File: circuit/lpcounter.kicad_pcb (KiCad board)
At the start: 2 copper layers, 52.1 x 45.7 mm, 19 parts, among them IC1 ATTINY85V-P, M1 SYN115, P1 CONN_01X08, P2 CONN_02X01

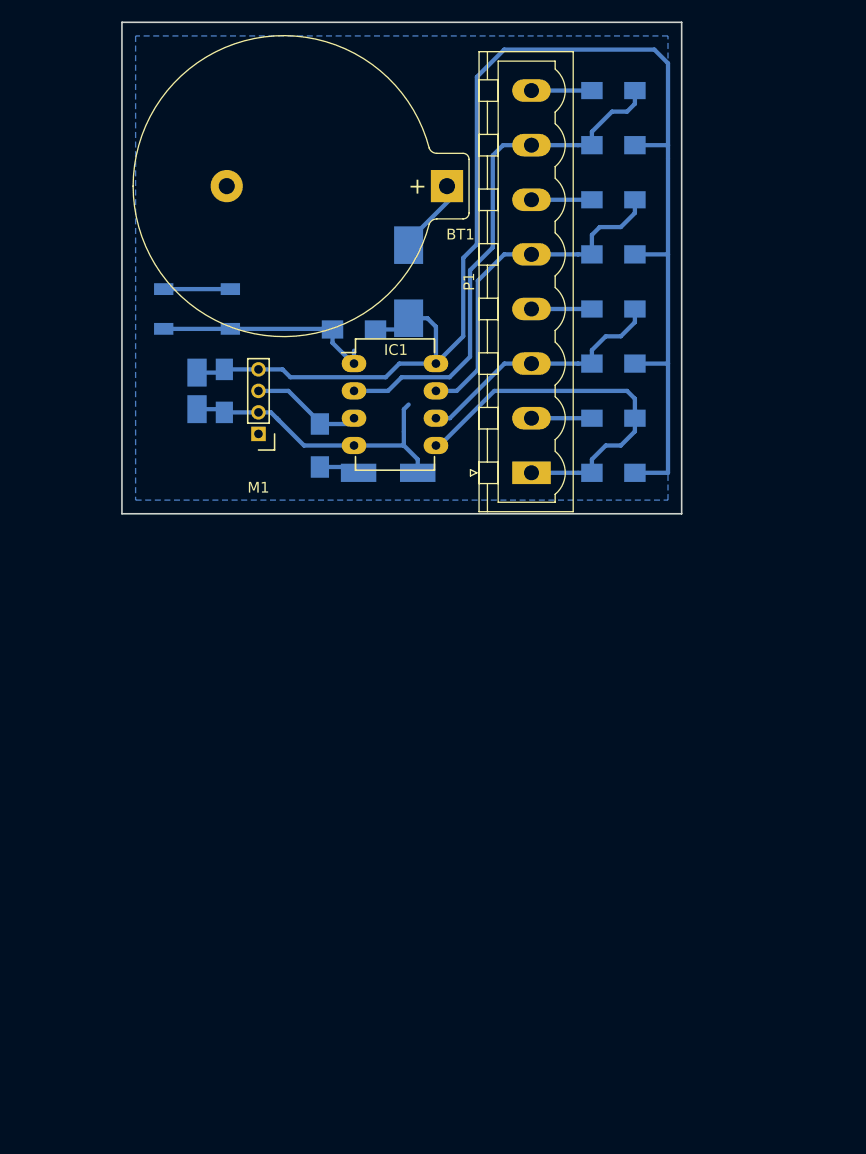
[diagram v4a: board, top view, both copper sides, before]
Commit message: correct footprint for SYN115, 4 screw holes, optimizing PCB drawing 18650 battery outiline
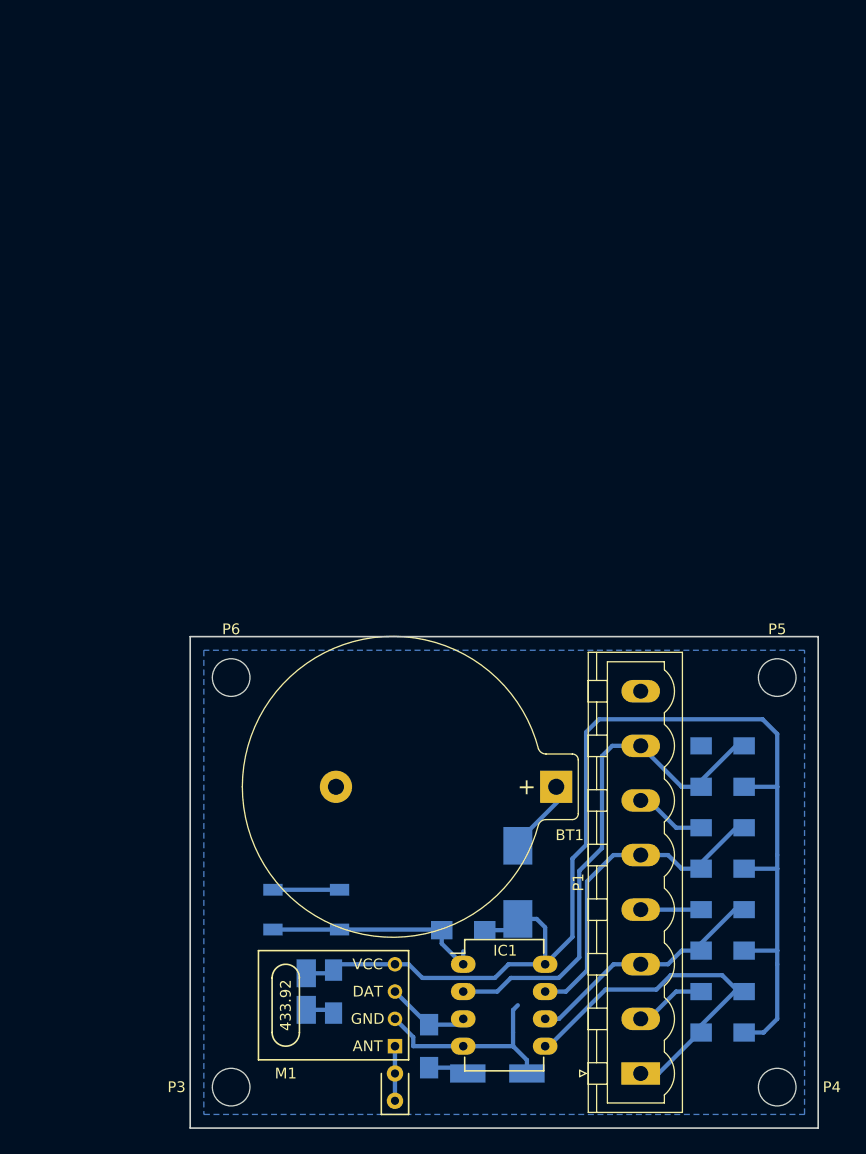
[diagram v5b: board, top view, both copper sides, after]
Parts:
- added P3: Hole_3.5mm, Mounting_Holes:MountingHole_3.5mm, F.Cu at (152.4, 119.4)
- added P4: Hole_3.5mm, Mounting_Holes:MountingHole_3.5mm, F.Cu at (203.2, 119.4)
- added P5: Hole_3.5mm, Mounting_Holes:MountingHole_3.5mm, F.Cu at (203.2, 81.3)
- added P6: Hole_3.5mm, Mounting_Holes:MountingHole_3.5mm, F.Cu at (152.4, 81.3)
- M1: footprint Pin_Headers:Pin_Header_Straight_1x04_Pitch2.00mm -> syn115:SYN115
- moved C4 61.8 mm to (198.1, 87.6)
- moved R4 60.5 mm to (198.1, 91.4)
- moved C3 59.3 mm to (198.1, 95.2)
- moved R3 58.0 mm to (198.1, 99.1)
- moved C6 56.8 mm to (161.9, 110.5)
- moved C2 56.8 mm to (198.1, 102.9)
- moved D2 56.8 mm to (177.2, 118.1)
- moved IC1 56.8 mm to (174.0, 108.0)
- moved P1 56.8 mm to (190.5, 118.1)
- moved P2 56.8 mm to (159.4, 102.9)
- moved R6 56.8 mm to (174.0, 104.8)
- moved BT1 56.8 mm to (182.6, 91.4)
- moved C5 56.8 mm to (159.4, 110.5)
- moved D1 56.8 mm to (179.1, 100.3)
- moved R5 56.8 mm to (170.8, 115.6)
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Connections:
- M1 pad 1: (no net) -> /ANT
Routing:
- net +3V3: track 131.4 -> 115.2 mm
- net GND: track 57.4 -> 48.4 mm
- net /ANT: track 0.00 -> 5.08 mm
- net /OUT: track 10.5 -> 8.00 mm
- net /IN2: track 32.7 -> 31.0 mm
- net /IN1: track 24.3 -> 23.1 mm
- net /IN0: track 36.1 -> 35.1 mm
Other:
- board size 52.1 x 45.7 mm -> 58.4 x 45.7 mm
- net class Default: clearance 0.2 -> 0.19
- rule trace_clearance: 0.2 -> 0.19

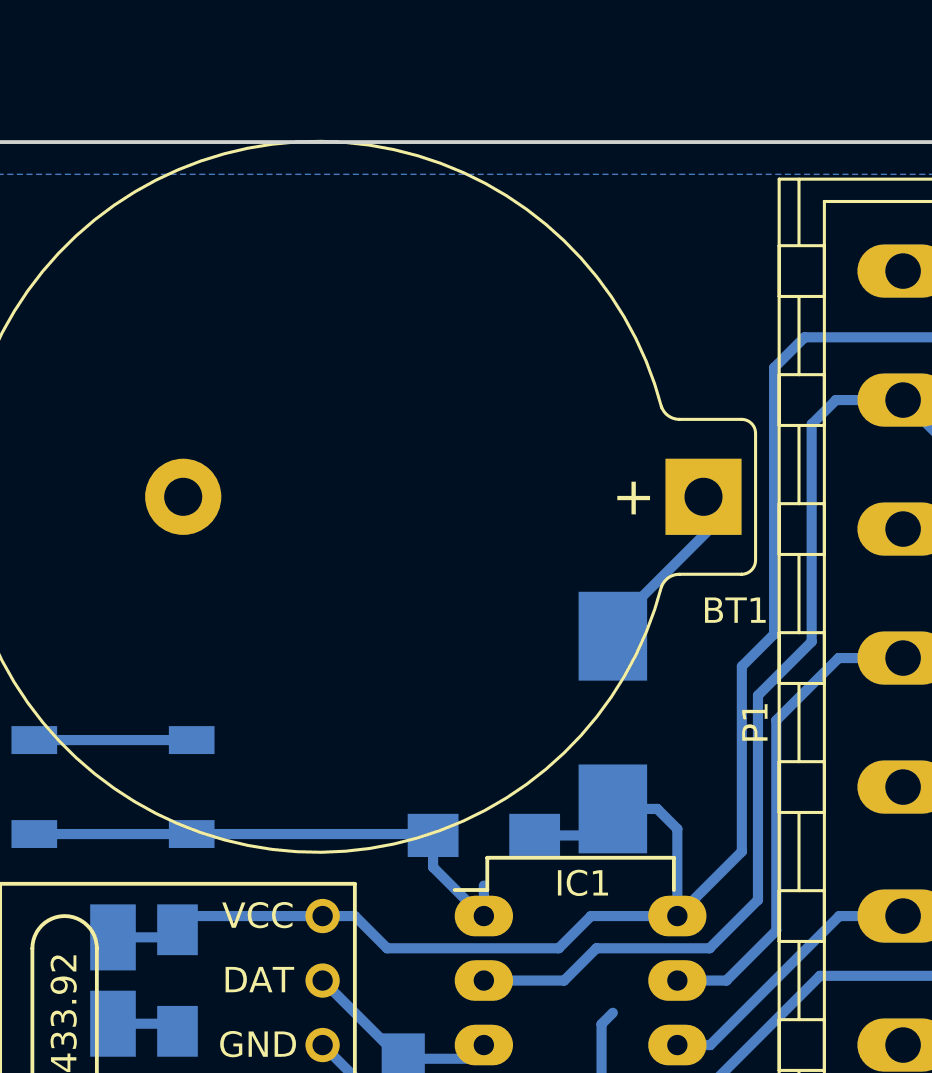
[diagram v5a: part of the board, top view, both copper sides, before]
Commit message: 3V battery connected direct, 3.7V battery connect in series with diode 1N4147
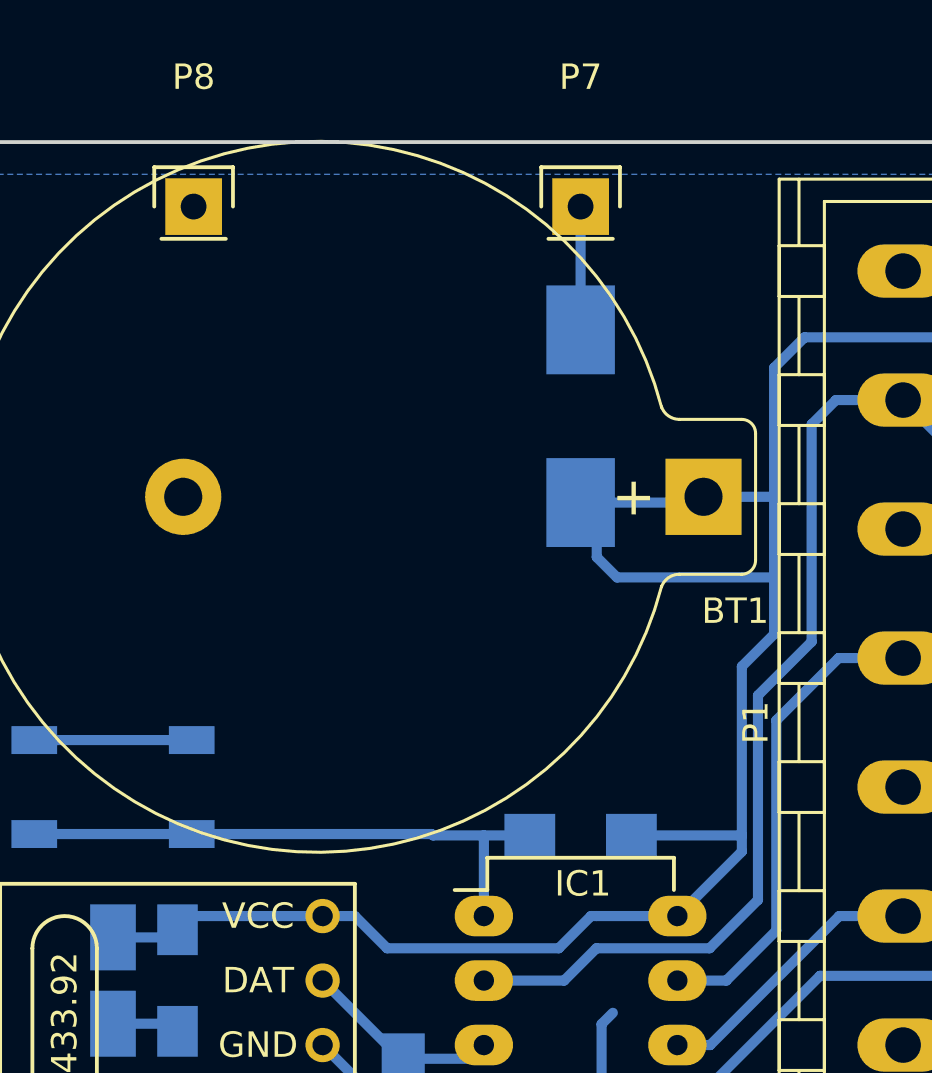
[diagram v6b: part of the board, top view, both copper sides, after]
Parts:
- added P7: BAT+, Pin_Headers:Pin_Header_Straight_1x01, F.Cu at (177.8, 80.0)
- added P8: BAT-, Pin_Headers:Pin_Header_Straight_1x01, F.Cu at (162.6, 80.0)
- BT1: value 3.7V -> CR2032
- moved D1 12.1 mm to (177.8, 88.3)
- moved R6 3.81 mm to (177.8, 104.8)
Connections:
- BT1 pad 1: Net-(BT1-Pad1) -> +3V3
- D1 pad 2: Net-(BT1-Pad1) -> Net-(D1-Pad2)
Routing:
- net +3V3: track 115.2 -> 126.0 mm
- net Net-(BT1-Pad1): track 7.86 -> 0.00 mm
- net Net-(D1-Pad2): track 0.00 -> 4.85 mm
- net /RESETn: track 21.1 -> 22.9 mm

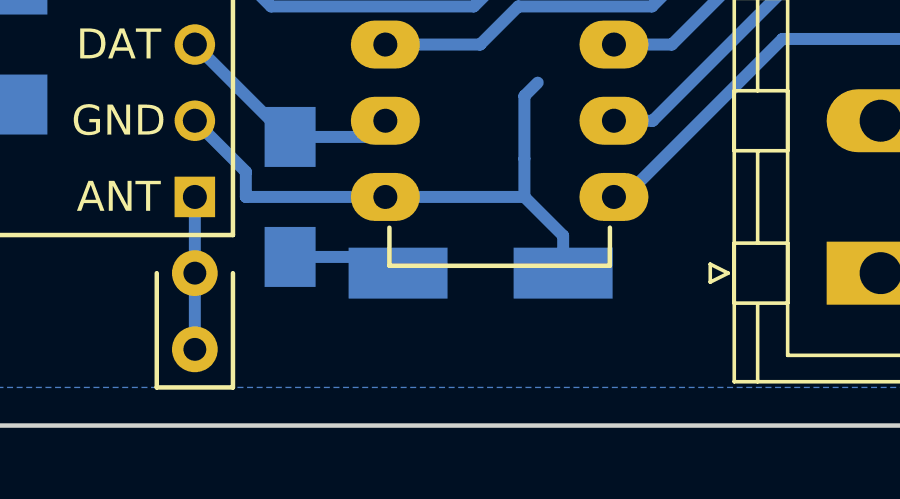
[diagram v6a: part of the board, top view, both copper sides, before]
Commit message: placeholder for both SMD and TH LED
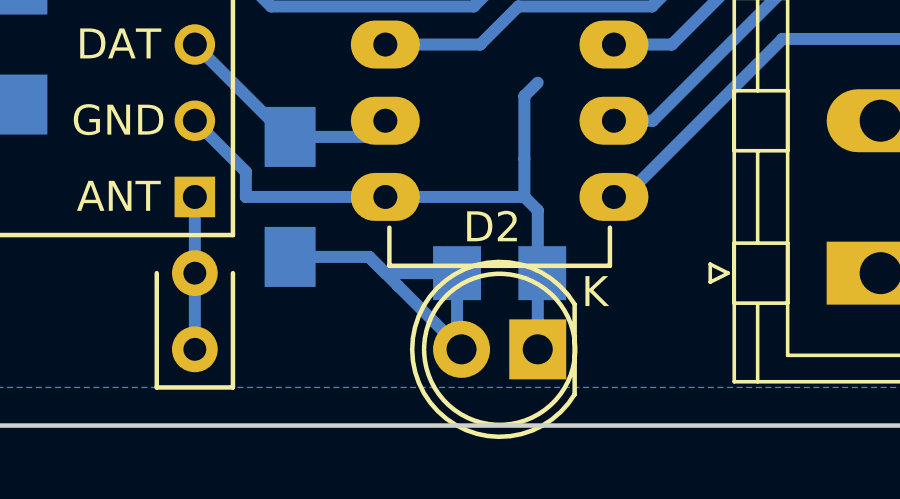
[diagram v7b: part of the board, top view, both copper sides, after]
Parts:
- added D3: ORANGE, LEDs:LED_1206, B.Cu at (177.8, 118.1)
- D2: footprint Diodes_SMD:MiniMELF_Handsoldering -> LEDs:LED-5MM; moved to F.Cu
- moved D2 3.18 mm to (179.1, 120.7)
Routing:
- net /LED: track 4.20 -> 12.7 mm
- net GND: track 48.4 -> 50.6 mm
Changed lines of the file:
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@@
 (kicad_pcb (version 4) (host pcbnew 4.0.5+dfsg1-4)
   (general
-    (links 51)
+    (links 53)
     (no_connects 0)
     (area 148.514999 77.394999 207.085001 123.265001)
     (thickness 1.6)
     (drawings 21)
-    (tracks 128)
+    (tracks 130)
     (zones 0)
-    (modules 25)
+    (modules 26)
     (nets 12)
   )
@@
       (scale (xyz 1 1 1))
       (rotate (xyz 0 0 0))
-    )
-  )
-  (module Diodes_SMD:MiniMELF_Handsoldering (layer B.Cu)
-    (at 177.165 118.11 180)
-    (descr "Diode Mini-MELF Handsoldering")
-    (tags "Diode Mini-MELF Handsoldering")
-    (attr smd)
-    (fp_text reference D2 (at 0 2.54 180) (layer B.SilkS)
-      (effects (font (size 1 1) (thickness 0.15)) (justify mirror))
-    )
-    (fp_text value ORANGE (at 0 -3.81 180) (layer B.Fab)
-      (effects (font (size 1 1) (thickness 0.15)) (justify mirror))
-    )
-    (fp_line (start -4.55 1) (end 4.55 1) (layer B.CrtYd) (width 0.05))
-    (fp_line (start 4.55 1) (end 4.55 -1) (layer B.CrtYd) (width 0.05))
-    (fp_line (start 4.55 -1) (end -4.55 -1) (layer B.CrtYd) (width 0.05))
-    (fp_line (start -4.55 -1) (end -4.55 1) (layer B.CrtYd) (width 0.05))
-    (fp_line (start -0.49958 0) (end -0.64944 0) (layer B.SilkS) (width 0.15))
-    (fp_line (start 0.34878 0) (end 0.54944 0) (layer B.SilkS) (width 0.15))
-    (fp_line (start -0.49958 0) (end -0.49958 -0.7493) (layer B.SilkS) (width 0.15))
-    (fp_line (start -0.49958 0) (end -0.49958 0.70104) (layer B.SilkS) (width 0.15))
-    (fp_line (start -0.49958 0) (end 0.34878 0.70104) (layer B.SilkS) (width 0.15))
-    (fp_line (start 0.34878 0.70104) (end 0.34878 -0.70104) (layer B.SilkS) (width 0.15))
-    (fp_line (start 0.34878 -0.70104) (end -0.49958 0) (layer B.SilkS) (width 0.15))
-    (fp_text user K (at -1.8 -1.85 180) (layer B.SilkS)
-      (effects (font (size 1 1) (thickness 0.15)) (justify mirror))
-    )
-    (fp_text user A (at 1.8 -1.85 180) (layer B.SilkS)
-      (effects (font (size 1 1) (thickness 0.15)) (justify mirror))
-    )
-    (pad 1 smd rect (at -2.75082 0 180) (size 3.29946 1.69926) (layers B.Cu B.Paste B.Mask)
-      (net 1 GND))
-    (pad 2 smd rect (at 2.75082 0 180) (size 3.29946 1.69926) (layers B.Cu B.Paste B.Mask)
-      (net 7 /LED))
-    (model Diodes_SMD.3dshapes/MiniMELF_Handsoldering.wrl
-      (at (xyz 0 0 0))
-      (scale (xyz 0.3937 0.3937 0.3937))
-      (rotate (xyz 0 0 180))
     )
   )
@@
     )
   )
+  (module LEDs:LED-5MM (layer F.Cu)
+    (at 179.07 120.65 180)
+    (descr "LED 5mm round vertical")
+    (tags "LED 5mm round vertical")
+    (fp_text reference D2 (at 1.524 4.064 180) (layer F.SilkS)
+      (effects (font (size 1 1) (thickness 0.15)))
+    )
+    (fp_text value ORANGE (at 1.524 -3.937 180) (layer F.Fab)
+      (effects (font (size 1 1) (thickness 0.15)))
+    )
+    (fp_line (start -1.5 -1.55) (end -1.5 1.55) (layer F.CrtYd) (width 0.05))
+    (fp_arc (start 1.3 0) (end -1.5 1.55) (angle -302) (layer F.CrtYd) (width 0.05))
+    (fp_arc (start 1.27 0) (end -1.23 -1.5) (angle 297.5) (layer F.SilkS) (width 0.15))
+    (fp_line (start -1.23 1.5) (end -1.23 -1.5) (layer F.SilkS) (width 0.15))
+    (fp_circle (center 1.27 0) (end 0.97 -2.5) (layer F.SilkS) (width 0.15))
+    (fp_text user K (at -1.905 1.905 180) (layer F.SilkS)
+      (effects (font (size 1 1) (thickness 0.15)))
+    )
+    (pad 1 thru_hole rect (at 0 0 270) (size 2 1.9) (drill 1.00076) (layers *.Cu *.Mask)
+      (net 1 GND))
+    (pad 2 thru_hole circle (at 2.54 0 180) (size 1.9 1.9) (drill 1.00076) (layers *.Cu *.Mask)
+      (net 7 /LED))
+    (model LEDs.3dshapes/LED-5MM.wrl
+      (at (xyz 0.05 0 0))
+      (scale (xyz 1 1 1))
+      (rotate (xyz 0 0 90))
+    )
+  )
+  (module LEDs:LED_1206 (layer B.Cu)
+    (at 177.8 118.11 180)
+    (descr "LED 1206 smd package")
+    (tags "LED1206 SMD")
+    (attr smd)
+    (fp_text reference D3 (at 0 2 180) (layer B.SilkS)
+      (effects (font (size 1 1) (thickness 0.15)) (justify mirror))
+    )
+    (fp_text value ORANGE (at 0 -2 180) (layer B.Fab)
+      (effects (font (size 1 1) (thickness 0.15)) (justify mirror))
+    )
+    (fp_line (start -0.5 0.5) (end -0.5 -0.5) (layer B.Fab) (width 0.15))
+    (fp_line (start -0.5 0) (end 0 0.5) (layer B.Fab) (width 0.15))
+    (fp_line (start 0 -0.5) (end -0.5 0) (layer B.Fab) (width 0.15))
+    (fp_line (start 0 0.5) (end 0 -0.5) (layer B.Fab) (width 0.15))
+    (fp_line (start -1.6 -0.8) (end -1.6 0.8) (layer B.Fab) (width 0.15))
+    (fp_line (start 1.6 -0.8) (end -1.6 -0.8) (layer B.Fab) (width 0.15))
+    (fp_line (start 1.6 0.8) (end 1.6 -0.8) (layer B.Fab) (width 0.15))
+    (fp_line (start -1.6 0.8) (end 1.6 0.8) (layer B.Fab) (width 0.15))
+    (fp_line (start -2.15 -1.05) (end 1.45 -1.05) (layer B.SilkS) (width 0.15))
+    (fp_line (start -2.15 1.05) (end 1.45 1.05) (layer B.SilkS) (width 0.15))
+    (fp_line (start -0.1 0.3) (end -0.1 -0.3) (layer B.SilkS) (width 0.15))
+    (fp_line (start -0.1 -0.3) (end -0.4 0) (layer B.SilkS) (width 0.15))
+    (fp_line (start -0.4 0) (end -0.2 0.2) (layer B.SilkS) (width 0.15))
+    (fp_line (start -0.2 0.2) (end -0.2 -0.05) (layer B.SilkS) (width 0.15))
+    (fp_line (start -0.2 -0.05) (end -0.25 0) (layer B.SilkS) (width 0.15))
+    (fp_line (start -0.5 0.5) (end -0.5 -0.5) (layer B.SilkS) (width 0.15))
+    (fp_line (start 0 0) (end 0.5 0) (layer B.SilkS) (width 0.15))
+    (fp_line (start -0.5 0) (end 0 0.5) (layer B.SilkS) (width 0.15))
+    (fp_line (start 0 0.5) (end 0 -0.5) (layer B.SilkS) (width 0.15))
+    (fp_line (start 0 -0.5) (end -0.5 0) (layer B.SilkS) (width 0.15))
+    (fp_line (start 2.5 1.25) (end -2.5 1.25) (layer B.CrtYd) (width 0.05))
+    (fp_line (start -2.5 1.25) (end -2.5 -1.25) (layer B.CrtYd) (width 0.05))
+    (fp_line (start -2.5 -1.25) (end 2.5 -1.25) (layer B.CrtYd) (width 0.05))
+    (fp_line (start 2.5 -1.25) (end 2.5 1.25) (layer B.CrtYd) (width 0.05))
+    (pad 2 smd rect (at 1.41986 0) (size 1.59766 1.80086) (layers B.Cu B.Paste B.Mask)
+      (net 7 /LED))
+    (pad 1 smd rect (at -1.41986 0) (size 1.59766 1.80086) (layers B.Cu B.Paste B.Mask)
+      (net 1 GND))
+    (model LEDs.3dshapes/LED_1206.wrl
+      (at (xyz 0 0 0))
+      (scale (xyz 1 1 1))
+      (rotate (xyz 0 0 180))
+    )
+  )
   (gr_circle (center 177.8 63.5) (end 179.07 62.23) (layer Eco2.User) (width 0.2))
   (gr_line (start 209.55 53.34) (end 142.24 53.34) (layer Eco2.User) (width 0.2))
@@
   (gr_line (start 207.01 77.47) (end 207.01 123.19) (layer Edge.Cuts) (width 0.15))
   (gr_line (start 148.59 77.47) (end 207.01 77.47) (layer Edge.Cuts) (width 0.15))
+  (segment (start 179.07 120.65) (end 179.07 116.015) (width 0.4) (layer B.Cu) (net 1))
+  (segment (start 179.07 116.015) (end 178.625 115.57) (width 0.4) (layer B.Cu) (net 1))
   (segment (start 196.12 87.42) (end 196.12 87.63) (width 0.4) (layer B.Cu) (net 1))
   (segment (start 193.79 95.25) (end 196.12 95.25) (width 0.4) (layer B.Cu) (net 1))
@@
   (segment (start 169.34 115.57) (end 173.99 115.57) (width 0.4) (layer B.Cu) (net 1))
   (segment (start 173.99 115.57) (end 178.625 115.57) (width 0.4) (layer B.Cu) (net 1))
-  (segment (start 179.916 116.8604) (end 179.916 118.11) (width 0.4) (layer B.Cu) (net 1))
-  (segment (start 178.625 115.57) (end 179.916 116.8604) (width 0.4) (layer B.Cu) (net 1))
   (segment (start 181.61 115.57) (end 181.96 115.57) (width 0.4) (layer B.Cu) (net 2))
   (segment (start 181.96 115.57) (end 187.225905 110.304095) (width 0.4) (layer B.Cu) (net 2))
@@
   (segment (start 161.625 108.79) (end 161.925 108.49) (width 0.4) (layer B.Cu) (net 6))
   (segment (start 159.385 108.79) (end 161.625 108.79) (width 0.4) (layer B.Cu) (net 6))
-  (segment (start 173.874 117.57) (end 174.144 117.84) (width 0.4) (layer B.Cu) (net 7))
-  (segment (start 170.815 117.57) (end 173.874 117.57) (width 0.4) (layer B.Cu) (net 7))
-  (segment (start 174.144 117.84) (end 174.414 118.11) (width 0.4) (layer B.Cu) (net 7))
-  (segment (start 174.1442 117.84) (end 174.4142 118.11) (width 0.4) (layer B.Cu) (net 7))
-  (segment (start 174.144 117.84) (end 174.1442 117.84) (width 0.4) (layer B.Cu) (net 7))
+  (segment (start 176.38014 118.11) (end 176.38014 120.50014) (width 0.4) (layer B.Cu) (net 7))
+  (segment (start 176.38014 120.50014) (end 176.53 120.65) (width 0.4) (layer B.Cu) (net 7))
+  (segment (start 176.38014 118.11) (end 173.99 118.11) (width 0.4) (layer B.Cu) (net 7))
+  (segment (start 173.99 118.11) (end 173.45 117.57) (width 0.4) (layer B.Cu) (net 7))
+  (segment (start 170.815 117.57) (end 173.45 117.57) (width 0.4) (layer B.Cu) (net 7))
+  (segment (start 173.45 117.57) (end 174.414 118.534) (width 0.4) (layer B.Cu) (net 7))
+  (segment (start 174.414 118.534) (end 176.53 120.65) (width 0.4) (layer B.Cu) (net 7))
   (segment (start 167.64 110.49) (end 170.72 113.57) (width 0.4) (layer B.Cu) (net 8))
   (segment (start 170.72 113.57) (end 170.815 113.57) (width 0.4) (layer B.Cu) (net 8))
